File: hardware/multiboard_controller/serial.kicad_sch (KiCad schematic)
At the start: 10 parts, among them U2 FT232HPQ-TRAY, U3 DG408DJZ, U5 DG408DJZ, Y1 12MHz

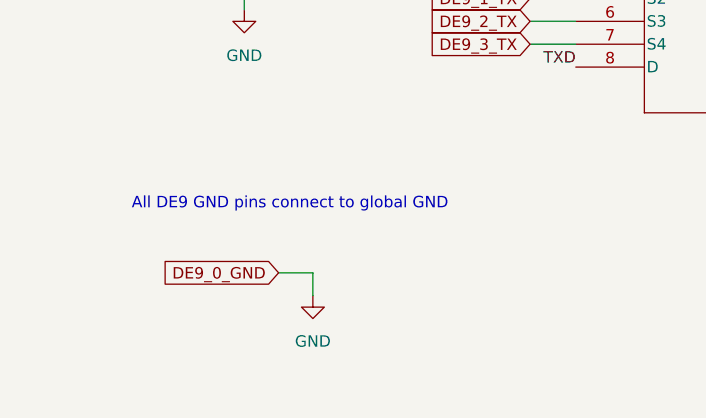
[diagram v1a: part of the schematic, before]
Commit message: Starting layout
Add serial ground connections, add footprint libraries, start layout.
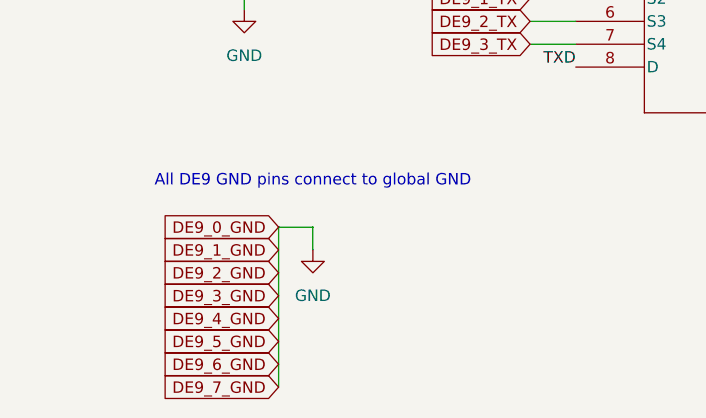
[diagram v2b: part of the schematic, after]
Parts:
- C5, C6: footprint (none) -> Capacitor_SMD:C_0402_1005Metric
- D1, D2: footprint (none) -> LED_SMD:LED_0805_2012Metric
- R29, R30: footprint (none) -> Resistor_SMD:R_0402_1005Metric
- Y1: footprint (none) -> Crystal:Crystal_SMD_2520-4Pin_2.5x2.0mm
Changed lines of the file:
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@@
+	(wire
+		(pts
+			(xy 46.99 176.53) (xy 46.99 194.31)
+		)
+		(stroke
+			(width 0)
+			(type default)
+		)
+	)
 	(wire
 		(pts
@@
 	(wire
 		(pts
-			(xy 50.8 181.61) (xy 50.8 184.15)
+			(xy 50.8 176.53) (xy 50.8 179.07)
 		)
 		(stroke
@@
 	(wire
 		(pts
-			(xy 46.99 181.61) (xy 50.8 181.61)
+			(xy 46.99 176.53) (xy 50.8 176.53)
 		)
 		(stroke
@@
 	(text "All DE9 GND pins connect to global GND"
 		(exclude_from_sim no)
-		(at 48.26 173.99 0)
+		(at 50.8 171.45 0)
 		(effects
 			(font
@@
 		)
 	)
+	(global_label "DE9_6_GND"
+		(shape input)
+		(at 46.99 191.77 180)
+		(fields_autoplaced yes)
+		(effects
+			(font
+				(size 1.27 1.27)
+			)
+			(justify right)
+		)
+		(property "Intersheetrefs" "${INTERSHEET_REFS}"
+			(at 33.3611 191.77 0)
+			(effects
+				(font
+					(size 1.27 1.27)
+				)
+				(justify right)
+				(hide yes)
+			)
+		)
+	)
 	(global_label "C2"
 		(shape input)
@@
 		)
 	)
+	(global_label "DE9_7_GND"
+		(shape input)
+		(at 46.99 194.31 180)
+		(fields_autoplaced yes)
+		(effects
+			(font
+				(size 1.27 1.27)
+			)
+			(justify right)
+		)
+		(property "Intersheetrefs" "${INTERSHEET_REFS}"
+			(at 33.3611 194.31 0)
+			(effects
+				(font
+					(size 1.27 1.27)
+				)
+				(justify right)
+				(hide yes)
+			)
+		)
+	)
 	(global_label "DE9_6_TX"
 		(shape input)
@@
 		)
 	)
+	(global_label "DE9_2_GND"
+		(shape input)
+		(at 46.99 181.61 180)
+		(fields_autoplaced yes)
+		(effects
+			(font
+				(size 1.27 1.27)
+			)
+			(justify right)
+		)
+		(property "Intersheetrefs" "${INTERSHEET_REFS}"
+			(at 33.3611 181.61 0)
+			(effects
+				(font
+					(size 1.27 1.27)
+				)
+				(justify right)
+				(hide yes)
+			)
+		)
+	)
 	(global_label "C0"
 		(shape input)
@@
 		)
 	)
+	(global_label "DE9_5_GND"
+		(shape input)
+		(at 46.99 189.23 180)
+		(fields_autoplaced yes)
+		(effects
+			(font
+				(size 1.27 1.27)
+			)
+			(justify right)
+		)
+		(property "Intersheetrefs" "${INTERSHEET_REFS}"
+			(at 33.3611 189.23 0)
+			(effects
+				(font
+					(size 1.27 1.27)
+				)
+				(justify right)
+				(hide yes)
+			)
+		)
+	)
 	(global_label "DE9_1_TX"
 		(shape input)
@@
 	(global_label "DE9_0_GND"
 		(shape input)
-		(at 46.99 181.61 180)
+		(at 46.99 176.53 180)
 		(fields_autoplaced yes)
 		(effects
@@
 		)
 		(property "Intersheetrefs" "${INTERSHEET_REFS}"
-			(at 33.3611 181.61 0)
+			(at 33.3611 176.53 0)
 			(effects
 				(font
@@
 		)
 	)
+	(global_label "DE9_1_GND"
+		(shape input)
+		(at 46.99 179.07 180)
+		(fields_autoplaced yes)
+		(effects
+			(font
+				(size 1.27 1.27)
+			)
+			(justify right)
+		)
+		(property "Intersheetrefs" "${INTERSHEET_REFS}"
+			(at 33.3611 179.07 0)
+			(effects
+				(font
+					(size 1.27 1.27)
+				)
+				(justify right)
+				(hide yes)
+			)
+		)
+	)
 	(global_label "C1"
 		(shape input)
@@
 		(property "Intersheetrefs" "${INTERSHEET_REFS}"
 			(at 185.8821 151.13 0)
+			(effects
+				(font
+					(size 1.27 1.27)
+				)
+				(justify right)
+				(hide yes)
+			)
+		)
+	)
+	(global_label "DE9_4_GND"
+		(shape input)
+		(at 46.99 186.69 180)
+		(fields_autoplaced yes)
+		(effects
+			(font
+				(size 1.27 1.27)
+			)
+			(justify right)
+		)
+		(property "Intersheetrefs" "${INTERSHEET_REFS}"
+			(at 33.3611 186.69 0)
+			(effects
+				(font
+					(size 1.27 1.27)
+				)
+				(justify right)
+				(hide yes)
+			)
+		)
+	)
+	(global_label "DE9_3_GND"
+		(shape input)
+		(at 46.99 184.15 180)
+		(fields_autoplaced yes)
+		(effects
+			(font
+				(size 1.27 1.27)
+			)
+			(justify right)
+		)
+		(property "Intersheetrefs" "${INTERSHEET_REFS}"
+			(at 33.3611 184.15 0)
 			(effects
 				(font
@@
 			)
 		)
-		(property "Footprint" ""
+		(property "Footprint" "Resistor_SMD:R_0402_1005Metric"
 			(at 164.846 72.644 90)
 			(effects
@@
 			)
 		)
-		(property "Footprint" ""
+		(property "Footprint" "Resistor_SMD:R_0402_1005Metric"
 			(at 176.276 72.644 90)
 			(effects
@@
 			)
 		)
-		(property "Footprint" ""
+		(property "Footprint" "Crystal:Crystal_SMD_2520-4Pin_2.5x2.0mm"
 			(at 29.21 67.31 0)
 			(effects
@@
 			)
 		)
-		(property "Footprint" ""
+		(property "Footprint" "Capacitor_SMD:C_0402_1005Metric"
 			(at 39.0652 81.28 0)
 			(effects
@@
 			)
 		)
-		(property "Footprint" ""
+		(property "Footprint" "Capacitor_SMD:C_0402_1005Metric"
 			(at 21.2852 81.28 0)
 			(effects
@@
 			)
 		)
-		(property "Footprint" ""
+		(property "Footprint" "LED_SMD:LED_0805_2012Metric"
 			(at 163.83 62.23 0)
 			(effects
@@
 			)
 		)
-		(property "Datasheet" "https://ftdichip.com/wp-content/uploads/2024/09/DS_FT233HP.pdf"
+		(property "Datasheet" "FT232HPQ-TRAY"
 			(at 90.17 25.4 0)
 			(effects
@@
 			)
 		)
-		(property "Datasheet" "https://www.renesas.com/en/document/dst/dg408-dg409-datasheet?r=493741"
+		(property "Datasheet" "DG408DJZ"
 			(at 80.01 140.97 0)
 			(effects
@@
 			)
 		)
-		(property "Footprint" ""
+		(property "Footprint" "LED_SMD:LED_0805_2012Metric"
 			(at 175.26 62.23 0)
 			(effects
@@
 	(symbol
 		(lib_id "power:GND")
-		(at 50.8 184.15 0)
+		(at 50.8 179.07 0)
 		(unit 1)
 		(exclude_from_sim no)
@@
 		(fields_autoplaced yes)
 		(property "Reference" "#PWR036"
-			(at 50.8 190.5 0)
+			(at 50.8 185.42 0)
 			(effects
 				(font
@@
 		)
 		(property "Value" "GND"
-			(at 50.8 189.23 0)
+			(at 50.8 184.15 0)
 			(effects
 				(font
@@
 		)
 		(property "Footprint" ""
-			(at 50.8 184.15 0)
+			(at 50.8 179.07 0)
 			(effects
 				(font
@@
 		)
 		(property "Datasheet" ""
-			(at 50.8 184.15 0)
+			(at 50.8 179.07 0)
 			(effects
 				(font
@@
 		)
 		(property "Description" "Power symbol creates a global label with name \"GND\" , ground"
-			(at 50.8 184.15 0)
-			(effects
-				(font
+			(at 50.8 179.07 0)
+			(effects
+				(font
